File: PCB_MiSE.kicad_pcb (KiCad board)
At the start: 2 copper layers, 35 parts, among them IC1 MSP430FR2355TPT, J1 WIFI, J2 Conn_01x03, J4 Clk read conn, J6 Display, J7 I2C read, J8 Conn_02x07_Odd_Even, SW1 SW_Push, SW2 SW_Push, SW3 SW_Push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

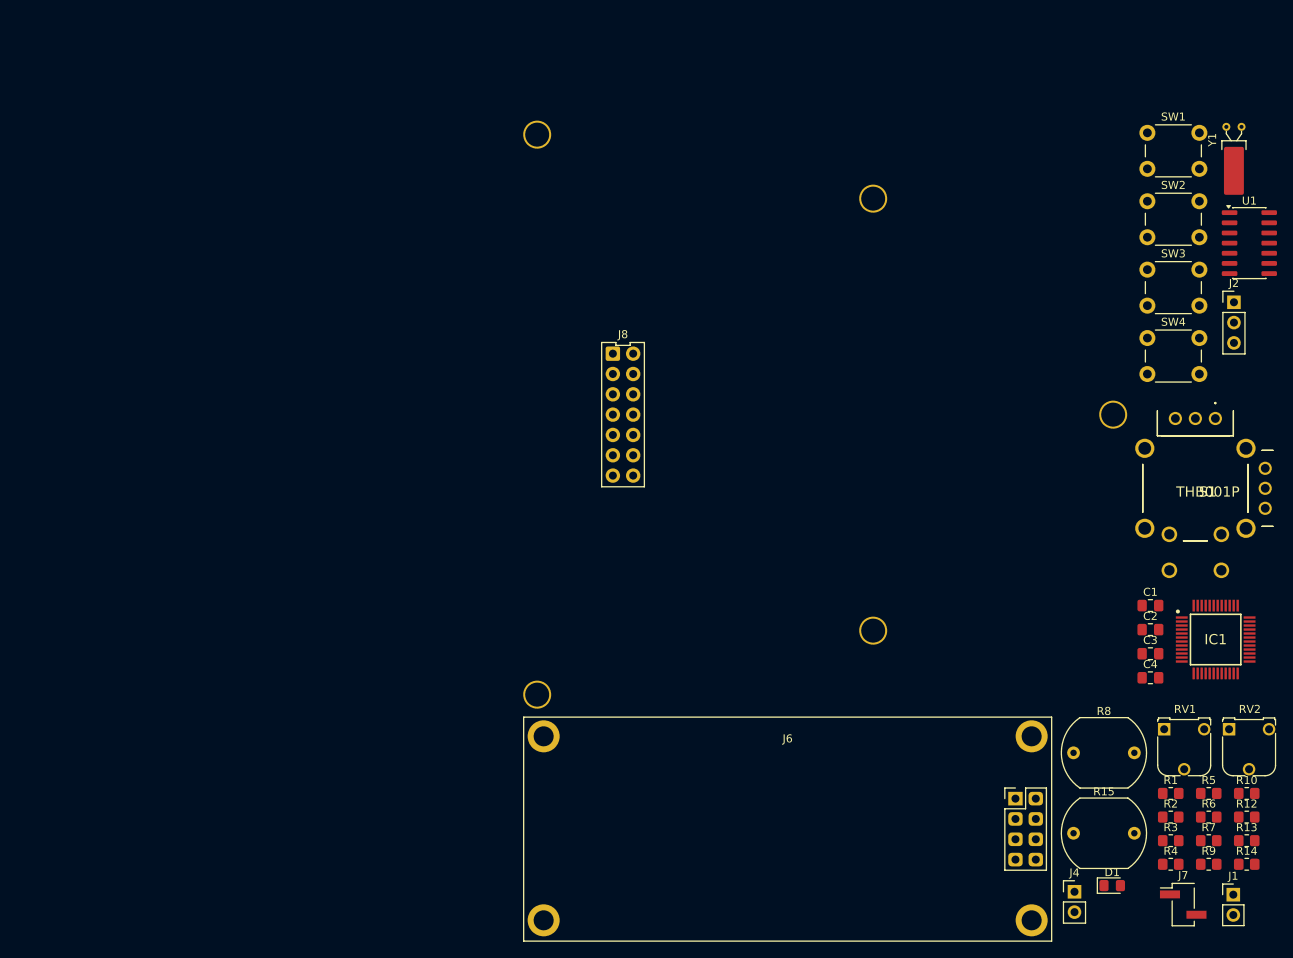
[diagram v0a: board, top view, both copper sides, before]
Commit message: Corrijo errores de diseño, DRC bien
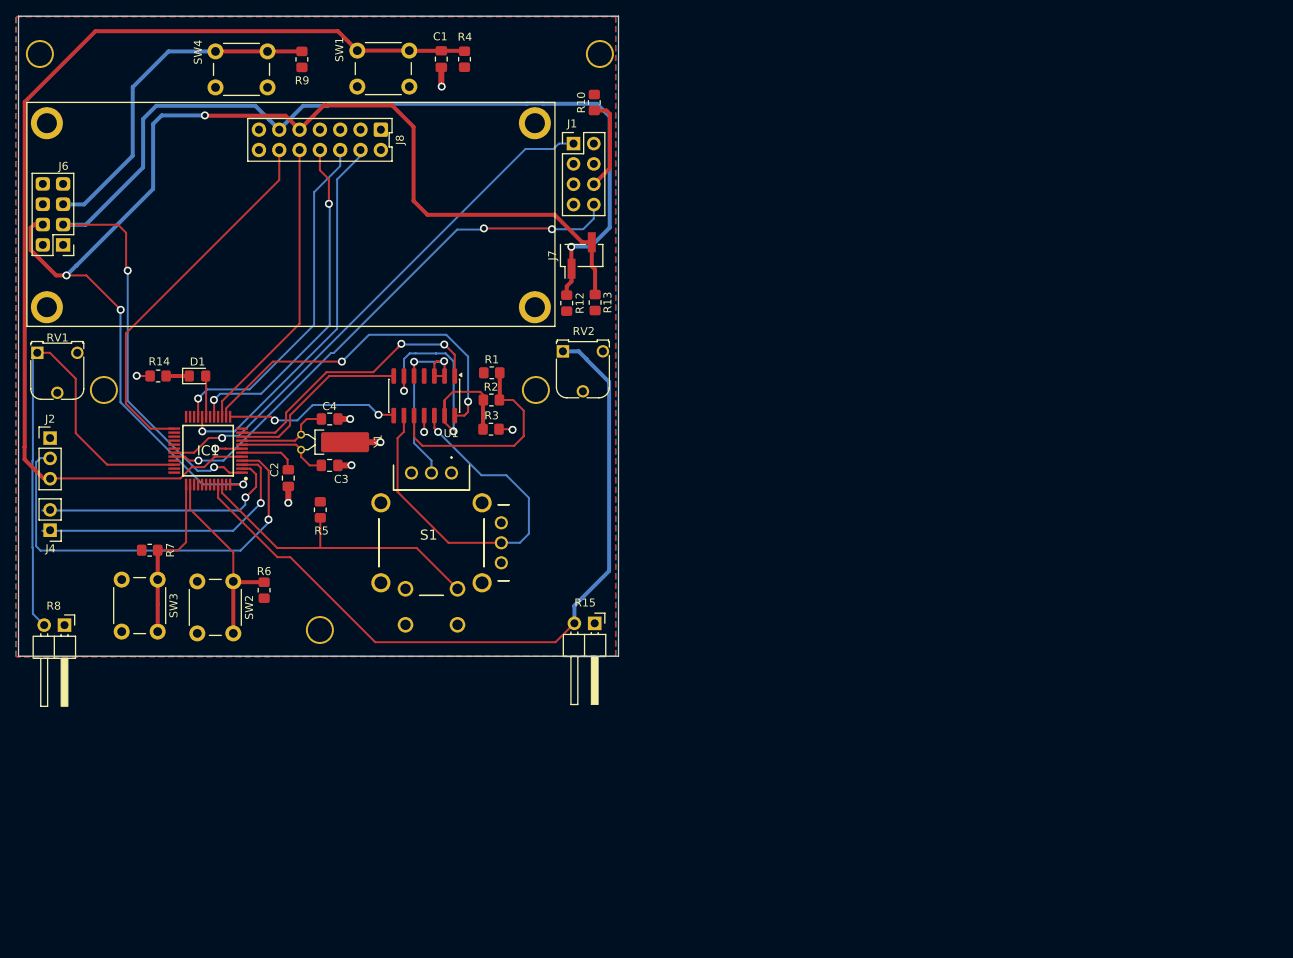
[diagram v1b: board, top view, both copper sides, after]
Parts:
- IC1: footprint MSP430:QFP50P900X900X160-48N -> Proyecto:QFP50P900X900X160-48N
- J1: footprint MSP430:LDR -> Connector_PinHeader_2.54mm:PinHeader_2x04_P2.54mm_Vertical
- J6: footprint MSP430:LCD_2x16_I2C(Midas) -> Proyecto:LCD_2x16_I2C(Midas)
- R15, R8: footprint OptoDevice:R_LDR_10x8.5mm_P7.6mm_Vertical -> Connector_PinHeader_2.54mm:PinHeader_1x02_P2.54mm_Horizontal
- RV1, RV2: footprint MSP430:Trimmer_MiSE -> Proyecto:Trimmer_MiSE
- S1: footprint MSP430:THB001P -> Proyecto:THB001P
- moved R9 151.6 mm to (78.6, 42.6), turned to 90 degrees
- moved R14 149.1 mm to (60.6, 82.2), turned to 180 degrees
- moved J2 149.0 mm to (47.1, 90.0)
- moved RV1 148.5 mm to (45.5, 79.3)
- moved R7 137.3 mm to (59.5, 104.0)
- moved J4 135.8 mm to (47.1, 101.5), turned to 180 degrees
- moved R4 133.9 mm to (98.9, 42.6), turned to 90 degrees
- moved D1 130.9 mm to (65.5, 82.2)
- moved SW3 129.6 mm to (60.5, 107.7), turned to -90 degrees
- moved IC1 128.1 mm to (66.8, 91.6), turned to 180 degrees
- moved R8 127.1 mm to (48.9, 113.4), turned to -90 degrees
- moved J1 125.0 mm to (112.5, 53.2)
- moved SW2 123.7 mm to (70.0, 107.9), turned to -90 degrees
- moved Y1 122.5 mm to (78.5, 91.4), turned to 90 degrees
- moved R6 121.4 mm to (73.8, 109.0), turned to 90 degrees
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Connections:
- net Net-(IC1-P2.6/MCLK/XOUT) renamed C-
- net Net-(IC1-P2.7/TB0CLK/XIN) renamed C+
- C2 pad 2: Net-(IC1-DVCC) -> GND
- IC1 pad 6: Net-(IC1-DVCC) -> VCC
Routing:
- net SDA: track 0.00 -> 155.7 mm, vias 0 -> 3
- net SCL: track 0.00 -> 151.6 mm, vias 0 -> 4
- net TDO/TDI: track 0.00 -> 133.7 mm
- net Net-(IC1-P3.2/OA2-): track 0.00 -> 94.7 mm
- net U0TXD: track 0.00 -> 67.0 mm, vias 0 -> 3
- net U0RXD: track 0.00 -> 65.9 mm, vias 0 -> 1
- net Net-(IC1-P1.4/UCA0STE/TCK/A4): track 0.00 -> 61.8 mm
- net TCK: track 0.00 -> 52.7 mm, vias 0 -> 1
- net Net-(S1-2'): track 0.00 -> 50.9 mm, vias 0 -> 1
- net P0: track 0.00 -> 47.6 mm, vias 0 -> 1
- net Net-(IC1-P4.1/UCA1CLK): track 0.00 -> 47.0 mm
- net GPIOl': track 0.00 -> 45.0 mm, vias 0 -> 2
- net P1: track 0.00 -> 43.8 mm, vias 0 -> 1
- net Net-(J6-Pin_5): track 0.00 -> 43.1 mm
- net P2: track 0.00 -> 42.9 mm, vias 0 -> 2
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- added copper zone on B.Cu, net GND
- added copper zone on F.Cu, net VCC
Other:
- board outline added: 75 x 80 mm

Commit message: Add files via upload
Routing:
- net GND: track 20.9 -> 47.7 mm, vias 9 -> 10
- net TDO/TDI: track 133.7 -> 115.3 mm, vias 0 -> 2
- net SDA: track 155.7 -> 137.3 mm, vias 3 -> 6
- net SCL: track 151.6 -> 158.5 mm, vias 4 -> 3
- net Net-(IC1-P3.2/OA2-): track 94.7 -> 88.5 mm, vias 0 -> 1
- net Net-(S1-2'): track 50.9 -> 46.9 mm
- net VCC: track 6.75 -> 3.60 mm, vias 0 -> 1
- net P1: track 43.8 -> 41.5 mm
- net P2: track 42.9 -> 40.7 mm
- net Net-(IC1-P3.1/OA2O): track 39.2 -> 37.3 mm, vias 0 -> 1
- net P0: track 47.6 -> 45.8 mm
- net CH_EN: track 11.7 -> 10.2 mm
- net Net-(IC1-P1.1/UCB0CLK/ACLK/OA0O/COMP0.1/A1): track 32.1 -> 30.6 mm
- net Net-(IC1-P4.1/UCA1CLK): track 47.0 -> 45.9 mm
- net Net-(IC1-P1.4/UCA0STE/TCK/A4): track 61.8 -> 60.9 mm, vias 0 -> 1
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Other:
- board size 75 x 80 mm -> 75 x 80.2 mm

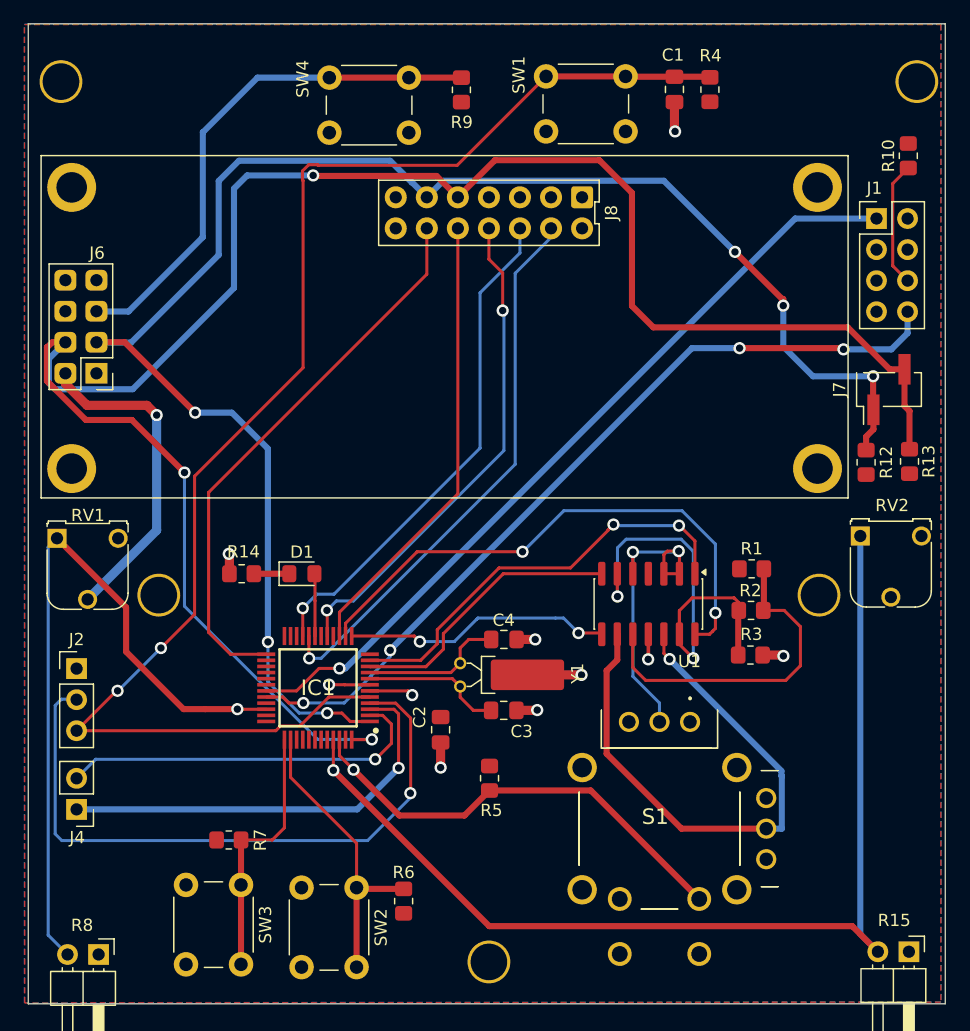
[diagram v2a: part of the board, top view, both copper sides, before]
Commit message: Arreglo diseño de vias
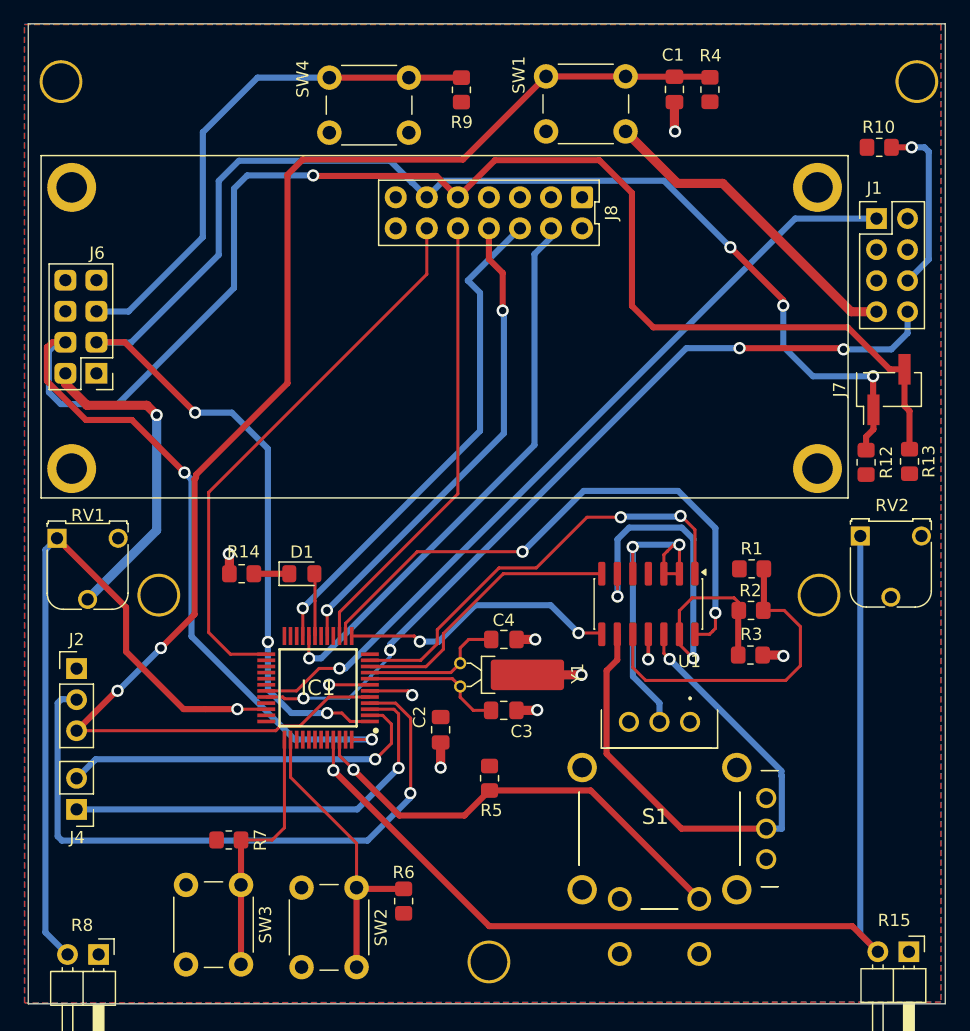
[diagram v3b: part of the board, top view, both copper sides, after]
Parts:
- moved R10 2.47 mm to (112.8, 47.4), turned to 0 degrees
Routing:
- net GND: track 47.7 -> 74.3 mm
- net CH_EN: track 10.2 -> 14.5 mm, vias 0 -> 1
- net SCL: track 158.5 -> 161.5 mm
- net Net-(U1A-+): track 26.5 -> 28.7 mm
- net GPIOl': track 45.0 -> 47.1 mm
- net Net-(U1B--): track 37.5 -> 39.3 mm
- net GPIOr: track 35.1 -> 36.4 mm
- net GPIOr': track 22.0 -> 22.9 mm
- net P2: track 40.7 -> 40.0 mm

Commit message: corrijo error
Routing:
- net P1: track 41.5 -> 40.7 mm
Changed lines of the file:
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@@
-	)
-	(segment
-		(start 80.1 59.25)
-		(end 79.095 58.245)
-		(width 0.5)
-		(layer "B.Cu")
-		(net 9)
 	)
 	(segment
@@
 	)
 	(segment
-		(start 79.095 58.245)
-		(end 83.365 53.975)
+		(start 80.1 70.545)
+		(end 80.1 57.24)
 		(width 0.5)
 		(layer "B.Cu")
@@
 	)
 	(segment
-		(start 80.1 70.545)
-		(end 80.1 59.25)
+		(start 80.1 57.24)
+		(end 83.365 53.975)
 		(width 0.5)
 		(layer "B.Cu")

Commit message: corrijo errores
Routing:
- net SCL: track 161.5 -> 162.7 mm, vias 3 -> 4
- net Net-(S1-2'): track 46.9 -> 47.7 mm
- net SDA: vias 6 -> 5

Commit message: corrijo las vías pequeñas
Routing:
- net Net-(IC1-P4.1/UCA1CLK): track 45.9 -> 46.0 mm, vias 0 -> 1
- net P8: vias 0 -> 1

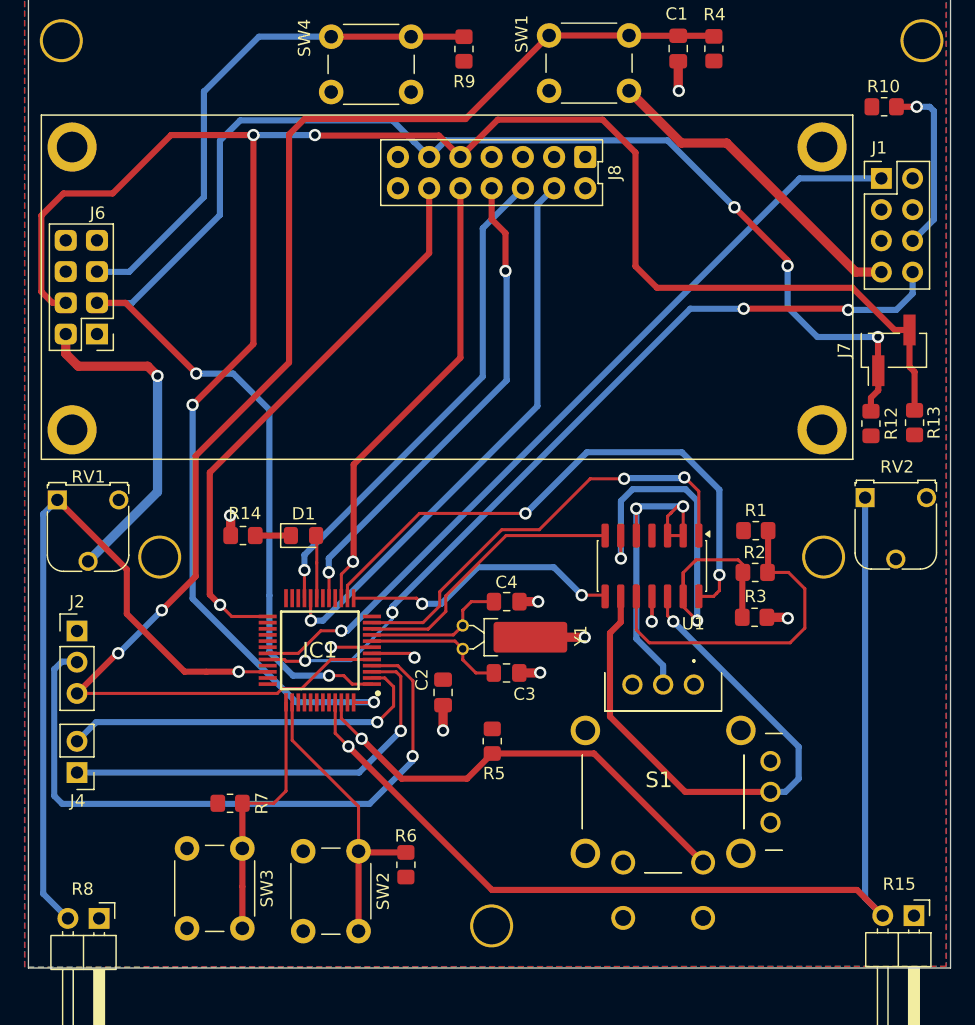
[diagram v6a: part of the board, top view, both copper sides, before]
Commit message: muevo los conectores segun dijo Pep
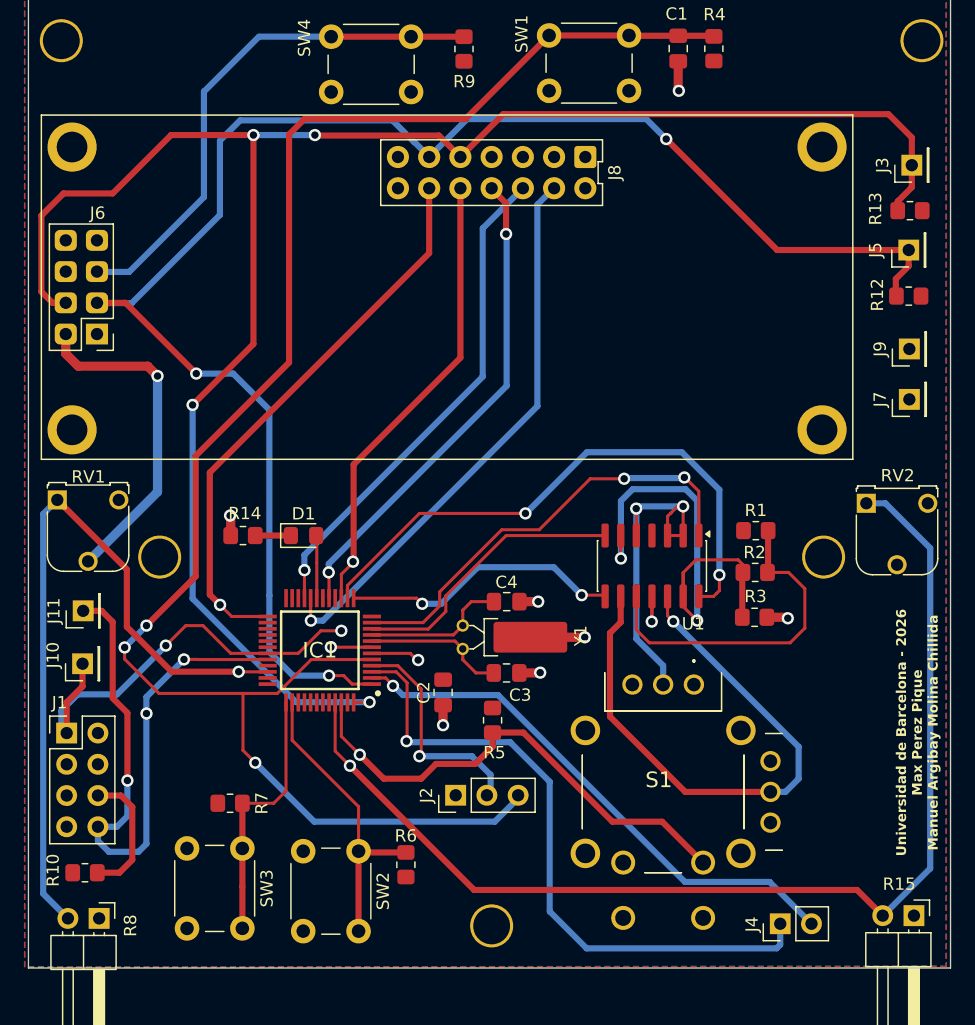
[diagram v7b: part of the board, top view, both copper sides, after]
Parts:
- added J10: Conn_01x01, Connector_PinHeader_2.54mm:PinHeader_1x01_P2.54mm_Vertical, F.Cu at (47.5, 92.7)
- added J11: Conn_01x01, Connector_PinHeader_2.54mm:PinHeader_1x01_P2.54mm_Vertical, F.Cu at (47.6, 88.3)
- added J3: Conn_01x01, Connector_PinHeader_2.54mm:PinHeader_1x01_P2.54mm_Vertical, F.Cu at (115.0, 52.1)
- added J5: Conn_01x01, Connector_PinHeader_2.54mm:PinHeader_1x01_P2.54mm_Vertical, F.Cu at (114.8, 59.0)
- added J9: Conn_01x01, Connector_PinHeader_2.54mm:PinHeader_1x01_P2.54mm_Vertical, F.Cu at (114.8, 67.0)
- J7: value I2C read -> Conn_01x01; footprint Connector_PinHeader_2.54mm:PinHeader_1x02_P2.54mm_Vertical_SMD_Pin1Left -> Connector_PinHeader_2.54mm:PinHeader_1x01_P2.54mm_Vertical
- moved R10 90.0 mm to (47.8, 109.7)
- moved J1 80.2 mm to (46.3, 98.3)
- moved J4 58.5 mm to (104.3, 113.8), turned to 90 degrees
- moved J2 33.6 mm to (77.9, 103.3), turned to 90 degrees
- moved R13 17.2 mm to (114.8, 55.8), turned to 180 degrees
- moved R12 10.8 mm to (114.8, 62.8), turned to 180 degrees
- moved J7 4.18 mm to (114.8, 71.2)
- moved R5 1.70 mm to (80.9, 97.2)
- moved RV2 0.47 mm to (111.3, 79.6)
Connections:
- J7 pad 1: SDA -> GND
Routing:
- net TCK: track 52.8 -> 18.5 mm
- net U0RXD: track 66.5 -> 35.9 mm, vias 1 -> 2
- net GND: track 74.7 -> 47.7 mm
- net TDO/TDI: track 115.7 -> 139.2 mm, vias 2 -> 3
- net Net-(IC1-P1.0/UCB0STE/SMCLK/COMP0.0/A0/VEREF+): track 34.9 -> 53.4 mm
- net U0TXD: track 67.6 -> 50.7 mm, vias 4 -> 3
- net Net-(IC1-P1.1/UCB0CLK/ACLK/OA0O/COMP0.1/A1): track 30.6 -> 44.1 mm
- net SCL: track 162.7 -> 150.4 mm
- net Net-(IC1-P3.2/OA2-): track 88.5 -> 93.0 mm
- net SDA: track 137.6 -> 133.4 mm, vias 5 -> 3
- net CH_EN: track 14.5 -> 10.8 mm, vias 1 -> 0
- net Net-(IC1-P3.1/OA2O): track 37.3 -> 40.2 mm
- net Net-(IC1-P1.4/UCA0STE/TCK/A4): track 61.2 -> 61.8 mm
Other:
- board text added: "Universidad de Barcelona - 2026 Max Perez Pique Manuel Argibay Molina Chillida"
